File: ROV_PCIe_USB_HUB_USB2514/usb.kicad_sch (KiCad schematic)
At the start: 62 parts, among them J2 61400826021, J3 691311500102, J4 692121430000, J5 61400826021, J6 61400826021, J7 629722000214, U10 TPS2051CDBV, U11 MIC5504-3.3YM5, U12 TPS2116DRL, U13 USB2514B_Bi, U5 TPS2051CDBV, U6 TPS2051CDBV, U8 TS3USB30EDGSR, U9 TPS2051CDBV, Y3 ABM8-24.000MHZ-B2-T

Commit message: updates
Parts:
- C35: Part Number CL21A106KOQNNNE -> CL21A106KOQNNNE
- C36: renamed from C60; Part Number CL05B104KB5NNNC -> CL05B104KO5NNNC
- C37: renamed from C59; Part Number CL05B104KB5NNNC -> CL05B104KO5NNNC
- C38: renamed from C58; Part Number CL05B104KB5NNNC -> CL05B104KO5NNNC
- C39: renamed from C57; Part Number CL05B104KB5NNNC -> CL05B104KO5NNNC
- C40: renamed from C53; Part Number CL21A106KOQNNNE -> CL21A106KOQNNNE
- C41: renamed from C54; Part Number CL05B104KB5NNNC -> CL05B104KO5NNNC
- C42: renamed from C55; Part Number CL05B104KB5NNNC -> CL05B104KO5NNNC
- C43: renamed from C36; Part Number CL21A106KOQNNNE -> CL21A106KOQNNNE
- C44: renamed from C37; Part Number CL21A106KOQNNNE -> CL21A106KOQNNNE
- C45: renamed from C40; Part Number CL05B104KB5NNNC -> CL05B104KO5NNNC
- C46: renamed from C41; Part Number CL21A106KOQNNNE -> CL21A106KOQNNNE
- C48: renamed from C49; value 18p -> 27p
- C49: renamed from C48; value 18p -> 27p
- C50: Part Number CL05B104KB5NNNC -> CL05B104KO5NNNC
- C51: renamed from C42; Part Number CL21A106KOQNNNE -> CL21A106KOQNNNE
- C52: renamed from C51; Part Number CL05B104KB5NNNC -> CL05B104KO5NNNC
- C53: renamed from C43; Part Number CL21A106KOQNNNE -> CL21A106KOQNNNE
- C54: renamed from C44; footprint Capacitor_SMD:C_0805_2012Metric -> Capacitor_SMD:C_0603_1608Metric; Part Number CL21B105KOFNNNE -> CL10B105KO8NNNC
- C55: renamed from C45; Part Number CL21A106KOQNNNE -> CL21A106KOQNNNE
- C56: renamed from C46; footprint Capacitor_SMD:C_0805_2012Metric -> Capacitor_SMD:C_0603_1608Metric; Part Number CL21B105KOFNNNE -> CL10B105KO8NNNC
- C57: renamed from C47; footprint Capacitor_SMD:C_0805_2012Metric -> Capacitor_SMD:C_0603_1608Metric; Part Number CL21B105KOFNNNE -> CL10B105KO8NNNC
- J3: renamed from J2; value 61400826021 -> USB-A-D-RA; Part Number 61400826021 -> USB-A-D-RA
- J4: value 692121430000 -> USB-A3-S-VT-CS5A; Part Number 692121430000 -> USB-A3-S-VT-CS5A
- J5, J6: value 61400826021 -> USB-A-D-RA; Part Number 61400826021 -> USB-A-D-RA
- R19: renamed from R38; Part Number AC0603FR-0710KL -> RC0603FR-0710KL
- R20: renamed from R19; Part Number AC0603FR-0710KL -> RC0603FR-0710KL
- R21: renamed from R37; value 12.0k 1% -> 12k; Part Number AC0603FR-0710KL -> RC0603FR-0712KL
- R22: renamed from R30; Part Number AC0603FR-0710KL -> RC0603FR-0710KL
- R23: renamed from R24; Part Number AC0603FR-075K1L -> RC0603FR-075K1L
- R24: renamed from R26; Part Number AC0603FR-0710KL -> RC0603FR-0710KL
- R25: Part Number AC0603FR-075K1L -> RC0603FR-075K1L
- R26: renamed from R27; Part Number AC0603FR-07330KL -> RC0603FR-07330KL
- R27: renamed from R28; Part Number AC0603FR-07100KL -> RC0603FR-07100KL
- R28: renamed from R31; Part Number AC0603FR-07470RL -> RC0603FR-07270RL
- R29: renamed from R32; Part Number AC0603FR-07470RL -> RC0603FR-07270RL
- R30: renamed from R29; Part Number AC0603FR-07100KL -> RC0603FR-07100KL
- R31: renamed from R33; Part Number AC0603FR-07470RL -> RC0603FR-07270RL
- R32: renamed from R36; Part Number AC0603FR-07470RL -> RC0603FR-07100RL
- R33: renamed from R34; Part Number AC0603FR-07470RL -> RC0603FR-07270RL
- R34: renamed from R35; Part Number AC0603FR-07470RL -> RC0603FR-07100RL
- U10, U5, U6, U9: value TPS2051CDBV -> TPS2051CDBVR; Part Number TPS2051CDBV -> TPS2051CDBVR
- U11: value MIC5504-3.3YM5 -> MIC5504-3.3YM5-TR; Part Number MIC5504-3.3YM5 -> MIC5504-3.3YM5-TR
- U8: renamed from U13; value USB2514B_Bi -> USB2514B/M2
- renumbered C52 to C47, D7 to D1, D8 to D2, D9 to D3, D12 to D4, D10 to D5, D11 to D6, FB3 to FB2, J3 to J2, U8 to U7, Y3 to Y2

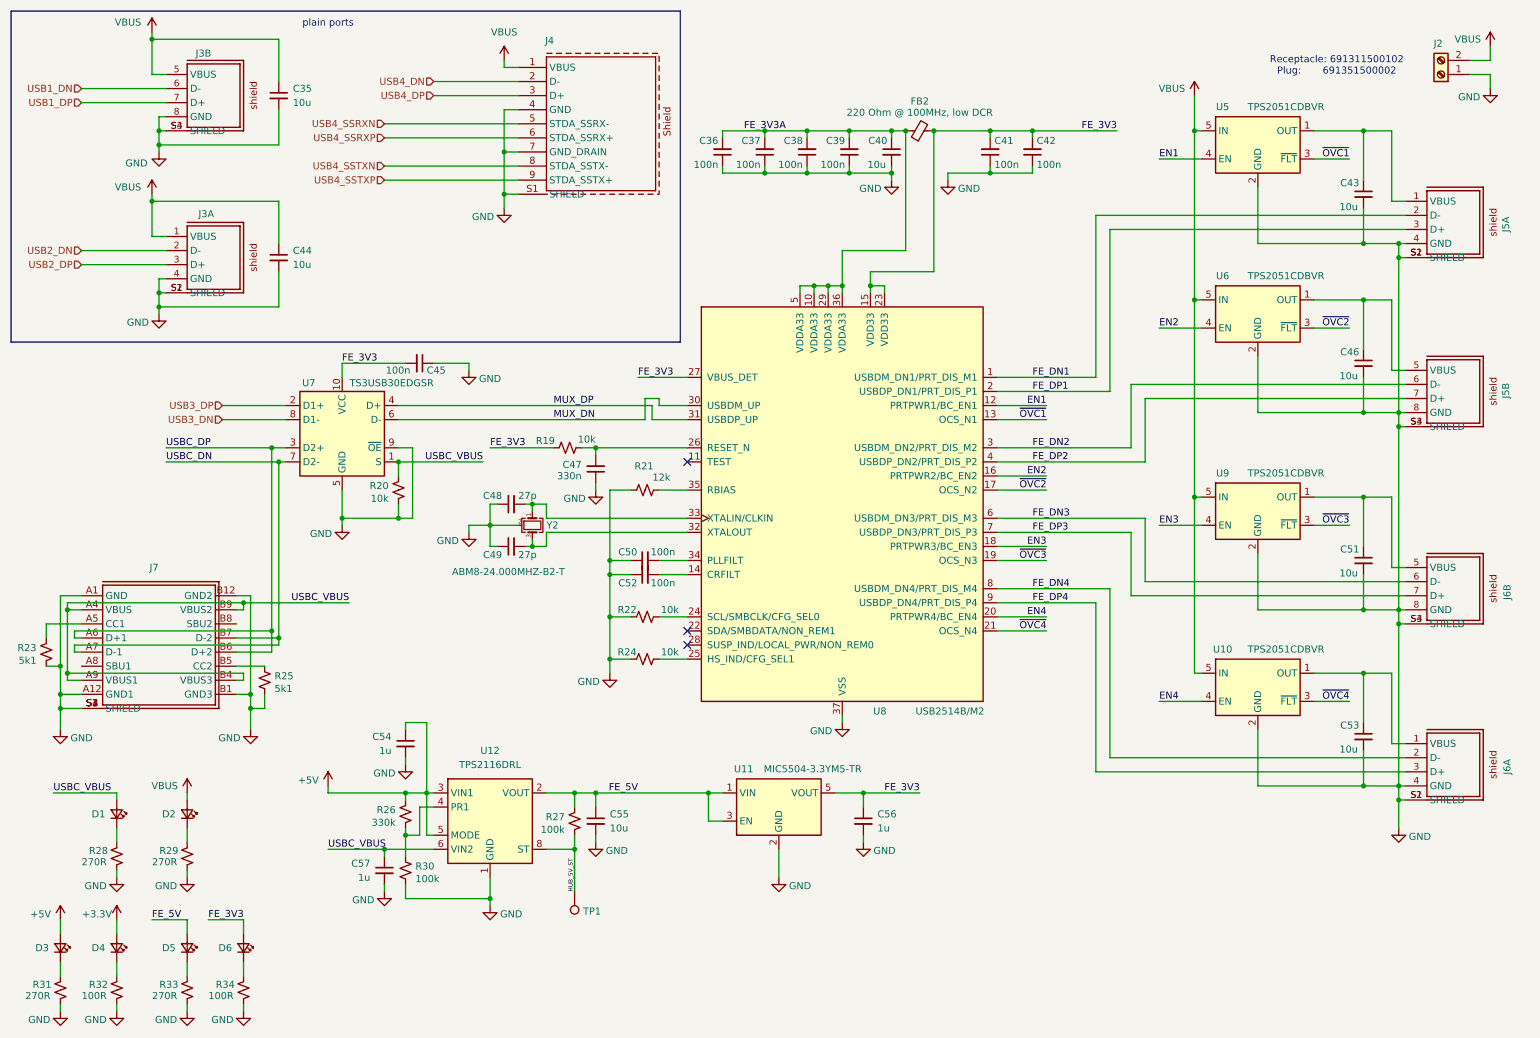
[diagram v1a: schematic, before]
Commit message: updates (fe1.1s board deprecated)
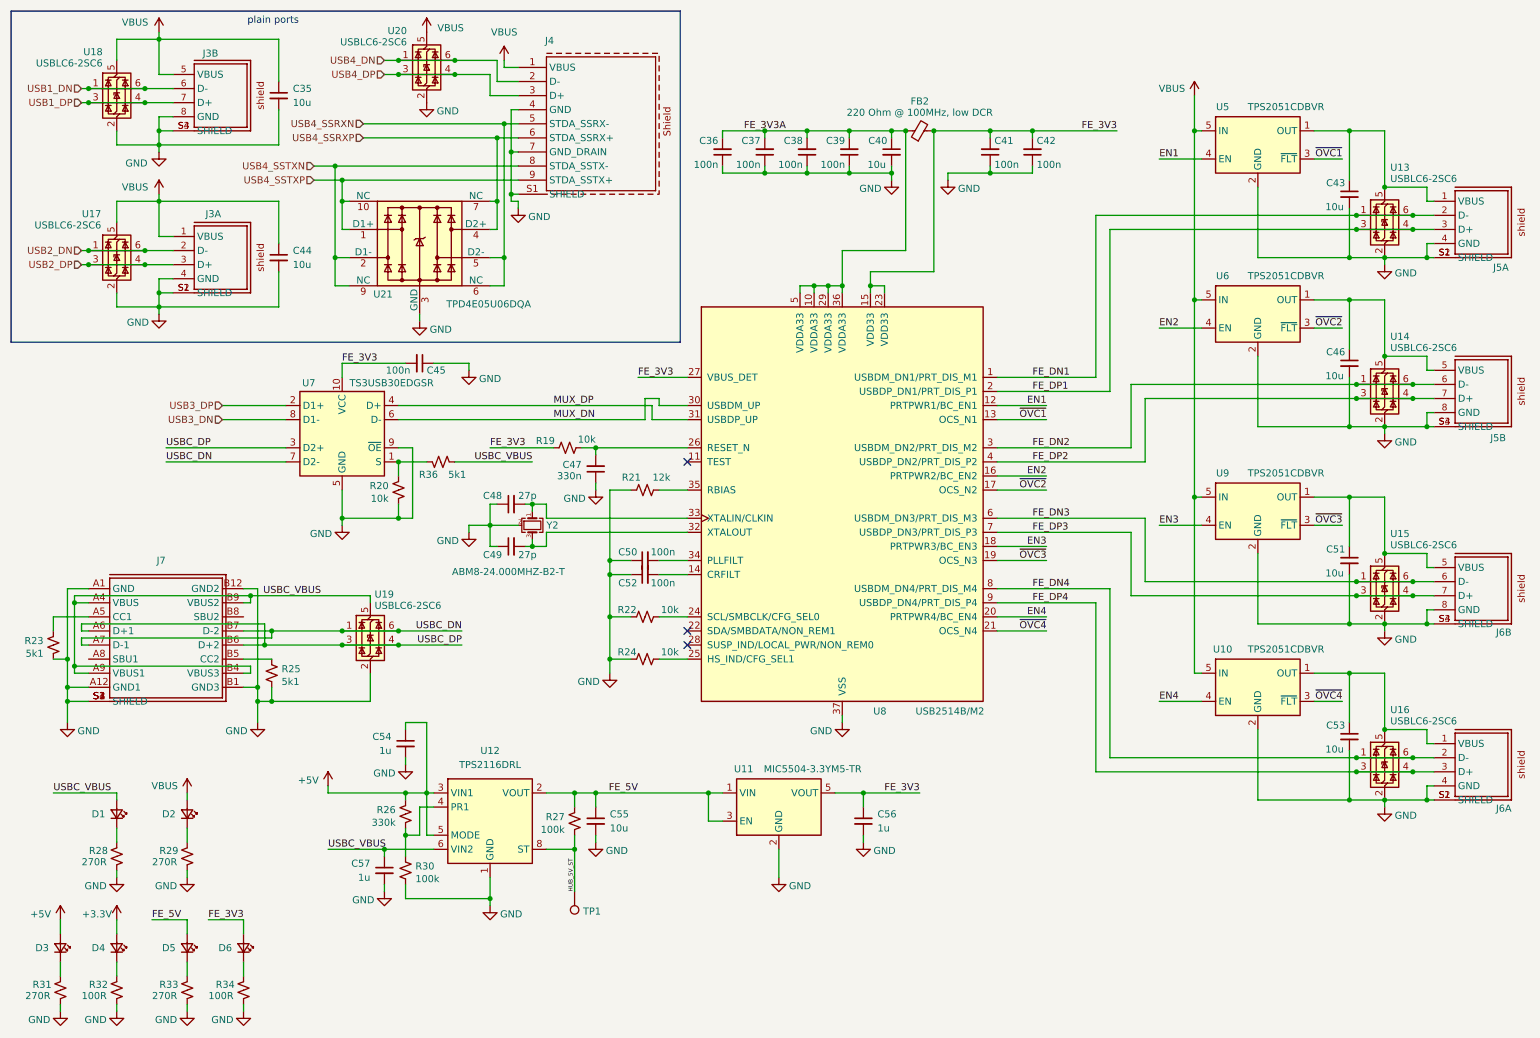
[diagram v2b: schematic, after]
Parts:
- removed J2: 691311500102, Connector_THT_Wurth:J_Wurth_WR-TBL_691311500102, symbol Connector:Screw_Terminal_01x02
- added R36: 5k1, Resistor_SMD:R_0603_1608Metric, symbol Device:R_Small_US
- added U13, U14, U15, U16, U17, U18, U19, U20: USBLC6-2SC6, Package_TO_SOT_SMD:SOT-23-6, symbol Power_Protection:USBLC6-2SC6
- added U21: TPD4E05U06DQA, Package_SON:USON-10_2.5x1.0mm_P0.5mm, symbol Power_Protection:TPD4E05U06DQA
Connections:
- net FE_DN1: now also U13.1 (I/O1), U13.6 (I/O1)
- net FE_DN2: now also U14.1 (I/O1), U14.6 (I/O1)
- net FE_DN3: now also U15.1 (I/O1), U15.6 (I/O1)
- net FE_DN4: now also U16.1 (I/O1), U16.6 (I/O1)
- net FE_DP1: now also U13.3 (I/O2), U13.4 (I/O2)
- net FE_DP2: now also U14.3 (I/O2), U14.4 (I/O2)
- net FE_DP3: now also U15.3 (I/O2), U15.4 (I/O2)
- net FE_DP4: now also U16.3 (I/O2), U16.4 (I/O2)
- net GND: now also U13.2 (GND), U14.2 (GND), U15.2 (GND), U16.2 (GND), U17.2 (GND), U18.2 (GND), U19.2 (GND), U20.2 (GND), U21.3 (GND), U21.8 (GND)
- net USB1_DN: now also U18.1 (I/O1), U18.6 (I/O1)
- net USB1_DP: now also U18.3 (I/O2), U18.4 (I/O2)
- net USB2_DN: now also U17.1 (I/O1), U17.6 (I/O1)
- net USB2_DP: now also U17.3 (I/O2), U17.4 (I/O2)
- net USB4_DN: now also U20.1 (I/O1), U20.6 (I/O1)
- net USB4_DP: now also U20.3 (I/O2), U20.4 (I/O2)
- net USB4_SSRXN: now also U21.5 (D2-), U21.6 (NC)
- net USB4_SSRXP: now also U21.4 (D2+), U21.7 (NC)
- net USB4_SSTXN: now also U21.2 (D1-), U21.9 (NC)
- net USB4_SSTXP: now also U21.1 (D1+), U21.10 (NC)
- net USBC_DN: now also U19.1 (I/O1), U19.6 (I/O1)
- net USBC_DP: now also U19.3 (I/O2), U19.4 (I/O2)
- net USBC_VBUS: now also R36.1, U19.5 (VBUS); no longer R20.2, U7.1 (S)
- net VBUS: now also U17.5 (VBUS), U18.5 (VBUS), U20.5 (VBUS)
- net at C53.1, J6.1 (VBUS), U10.1 (OUT): now also U16.5 (VBUS)
- net at C51.1, J6.5 (VBUS), U9.1 (OUT): now also U15.5 (VBUS)
- net at C46.1, J5.5 (VBUS), U6.1 (OUT): now also U14.5 (VBUS)
- net at C43.1, J5.1 (VBUS), U5.1 (OUT): now also U13.5 (VBUS)
- new net: R20.2, R36.2, U7.1 (S)
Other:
- note removed: "Receptacle: 691311500102 Plug: 691351500002"
- moved on the sheet: C43, C46, C51, C53, J3A, J3B, J5A, J5B, J6A, J6B, J7, R23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

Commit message: changes
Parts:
- C35, C40, C43, C44, C46, C51, C53, C55: Part Number CL21A106KOQNNNE -> CC0805KRX5R8BB106
- C36, C37, C38, C39, C41, C42, C45, C50, C52: Part Number CL05B104KO5NNNC -> CC0402KRX7R8BB104
- C47: Part Number CL05A334KQ5NNNC -> CC0402KPX5R6BB334
- C48, C49: Part Number CL05C180JB5NNNC -> CC0402JRNPO9BN270
- C54, C56, C57: Part Number CL10B105KO8NNNC -> CC0603KRX7R8BB105
- R21: value 12k -> 12k 1%
- R26: value 330k -> 10k; Part Number RC0603FR-07330KL -> RC0603FR-0710KL
- R30: value 100k -> 5k1; Part Number RC0603FR-07100KL -> RC0603FR-075K1L
- R36: Part Number RC0603FR-0710KL -> RC0603FR-075K1L
- U13, U14, U15, U16, U17, U18, U19, U20: Part Number (none) -> USBLC6-2SC6
- U21: Part Number (none) -> TPD4E05U06DQA
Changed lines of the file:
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@@
 			)
 		)
-		(property "Value" "330k"
+		(property "Value" "10k"
 			(at 82.042 159.004 0)
 			(show_name no)
@@
 			)
 		)
-		(property "Part Number" "RC0603FR-07330KL"
+		(property "Part Number" "RC0603FR-0710KL"
 			(at 83.82 157.48 0)
 			(hide yes)
@@
 			)
 		)
+		(property "Part Number" "USBLC6-2SC6"
+			(at 260.35 147.32 0)
+			(hide yes)
+			(show_name no)
+			(do_not_autoplace no)
+			(effects
+				(font
+					(size 1.27 1.27)
+				)
+			)
+		)
 		(pin "1"
 		)
@@
 			)
 		)
-		(property "Part Number" "CL05B104KO5NNNC"
+		(property "Part Number" "CC0402KRX7R8BB104"
 			(at 148.59 38.1 0)
 			(hide yes)
@@
 			)
 		)
-		(property "Part Number" "CL10B105KO8NNNC"
+		(property "Part Number" "CC0603KRX7R8BB105"
 			(at 166.37 158.75 0)
 			(hide yes)
@@
 			)
 		)
-		(property "Part Number" "CL21A106KOQNNNE "
+		(property "Part Number" "CC0805KRX5R8BB106"
 			(at 60.96 27.94 0)
 			(hide yes)
@@
 			)
 		)
-		(property "Part Number" "CL21A106KOQNNNE "
+		(property "Part Number" "CC0805KRX5R8BB106"
 			(at 254 143.51 0)
 			(hide yes)
@@
 			)
 		)
-		(property "Part Number" "CL05B104KO5NNNC"
+		(property "Part Number" "CC0402KRX7R8BB104"
 			(at 196.85 38.1 0)
 			(hide yes)
@@
 			)
 		)
+		(property "Part Number" "USBLC6-2SC6"
+			(at 260.35 80.01 0)
+			(hide yes)
+			(show_name no)
+			(do_not_autoplace no)
+			(effects
+				(font
+					(size 1.27 1.27)
+				)
+			)
+		)
 		(pin "1"
 		)
@@
 			)
 		)
-		(property "Part Number" "CL05A334KQ5NNNC"
+		(property "Part Number" "CC0402KPX5R6BB334"
 			(at 118.11 95.25 0)
 			(hide yes)
@@
 			)
 		)
-		(property "Part Number" "CL05B104KO5NNNC"
+		(property "Part Number" "CC0402KRX7R8BB104"
 			(at 156.21 38.1 0)
 			(hide yes)
@@
 			)
 		)
-		(property "Part Number" "CL05C180JB5NNNC"
+		(property "Part Number" "CC0402JRNPO9BN270"
 			(at 102.87 109.22 0)
 			(hide yes)
@@
 			)
 		)
-		(property "Part Number" "CL21A106KOQNNNE "
+		(property "Part Number" "CC0805KRX5R8BB106"
 			(at 254 76.2 0)
 			(hide yes)
@@
 			)
 		)
-		(property "Part Number" "CL21A106KOQNNNE "
+		(property "Part Number" "CC0805KRX5R8BB106"
 			(at 118.11 158.75 0)
 			(hide yes)
@@
 			)
 		)
+		(property "Part Number" "TPD4E05U06DQA"
+			(at 86.36 54.61 0)
+			(hide yes)
+			(show_name no)
+			(do_not_autoplace no)
+			(effects
+				(font
+					(size 1.27 1.27)
+				)
+			)
+		)
 		(pin "2"
 		)
@@
 			)
 		)
+		(property "Part Number" "USBLC6-2SC6"
+			(at 31.75 55.88 0)
+			(hide yes)
+			(show_name no)
+			(do_not_autoplace no)
+			(effects
+				(font
+					(size 1.27 1.27)
+				)
+			)
+		)
 		(pin "1"
 		)
@@
 			)
 		)
-		(property "Part Number" "CL05B104KO5NNNC"
+		(property "Part Number" "CC0402KRX7R8BB104"
 			(at 127 111.76 0)
 			(hide yes)
@@
 			)
 		)
-		(property "Part Number" "CL05C180JB5NNNC"
+		(property "Part Number" "CC0402JRNPO9BN270"
 			(at 102.87 101.6 0)
 			(hide yes)
@@
 			)
 		)
+		(property "Part Number" "USBLC6-2SC6"
+			(at 260.35 49.53 0)
+			(hide yes)
+			(show_name no)
+			(do_not_autoplace no)
+			(effects
+				(font
+					(size 1.27 1.27)
+				)
+			)
+		)
 		(pin "1"
 		)
@@
 			)
 		)
+		(property "Part Number" "USBLC6-2SC6"
+			(at 260.35 115.57 0)
+			(hide yes)
+			(show_name no)
+			(do_not_autoplace no)
+			(effects
+				(font
+					(size 1.27 1.27)
+				)
+			)
+		)
 		(pin "1"
 		)
@@
 			)
 		)
-		(property "Part Number" "CL21A106KOQNNNE "
+		(property "Part Number" "CC0805KRX5R8BB106"
 			(at 171.45 38.1 0)
 			(hide yes)
@@
 			)
 		)
-		(property "Part Number" "CL21A106KOQNNNE "
+		(property "Part Number" "CC0805KRX5R8BB106"
 			(at 60.96 57.15 0)
 			(hide yes)
@@
 			)
 		)
-		(property "Part Number" "CL05B104KO5NNNC"
+		(property "Part Number" "CC0402KRX7R8BB104"
 			(at 189.23 38.1 0)
 			(hide yes)
@@
 			)
 		)
+		(property "Part Number" "USBLC6-2SC6"
+			(at 87.63 21.59 0)
+			(hide yes)
+			(show_name no)
+			(do_not_autoplace no)
+			(effects
+				(font
+					(size 1.27 1.27)
+				)
+			)
+		)
 		(pin "1"
 		)
@@
 			)
 		)
+		(property "Part Number" "USBLC6-2SC6"
+			(at 31.75 26.67 0)
+			(hide yes)
+			(show_name no)
+			(do_not_autoplace no)
+			(effects
+				(font
+					(size 1.27 1.27)
+				)
+			)
+		)
 		(pin "1"
 		)
@@
 			)
 		)
-		(property "Part Number" "CL21A106KOQNNNE "
+		(property "Part Number" "CC0805KRX5R8BB106"
 			(at 254 45.72 0)
 			(hide yes)
@@
 			)
 		)
-		(property "Part Number" "CL05B104KO5NNNC"
+		(property "Part Number" "CC0402KRX7R8BB104"
 			(at 127 114.3 0)
 			(hide yes)
@@
 			)
 		)
-		(property "Value" "12k"
+		(property "Value" "12k 1%"
 			(at 131.572 96.774 90)
 			(show_name no)
@@
 			)
 		)
-		(property "Part Number" "RC0603FR-0710KL"
+		(property "Part Number" "RC0603FR-075K1L"
 			(at 90.17 93.98 0)
 			(hide yes)
@@
 			)
 		)
-		(property "Part Number" "CL05B104KO5NNNC"
+		(property "Part Number" "CC0402KRX7R8BB104"
 			(at 140.97 38.1 0)
 			(hide yes)
@@
 			)
 		)
-		(property "Part Number" "CL21A106KOQNNNE "
+		(property "Part Number" "CC0805KRX5R8BB106"
 			(at 254 111.76 0)
 			(hide yes)
@@
 			)
 		)
-		(property "Value" "100k"
+		(property "Value" "5k1"
 			(at 85.598 169.164 0)
 			(show_name no)
@@
 			)
 		)
-		(property "Part Number" "RC0603FR-07100KL"
+		(property "Part Number" "RC0603FR-075K1L"
 			(at 83.82 167.64 0)
 			(hide yes)
@@
 			)
 		)
+		(property "Part Number" "USBLC6-2SC6"
+			(at 77.47 124.46 0)
+			(hide yes)
+			(show_name no)
+			(do_not_autoplace no)
+			(effects
+				(font
+					(size 1.27 1.27)
+				)
+			)
+		)
 		(pin "1"
 		)
@@
 			)
 		)
-		(property "Part Number" "CL05B104KO5NNNC"
+		(property "Part Number" "CC0402KRX7R8BB104"
 			(at 86.36 76.2 0)
 			(hide yes)
@@
 			)
 		)
-		(property "Part Number" "CL10B105KO8NNNC"
+		(property "Part Number" "CC0603KRX7R8BB105"
 			(at 83.82 144.78 0)
 			(hide yes)
@@
 			)
 		)
-		(property "Part Number" "CL10B105KO8NNNC"
+		(property "Part Number" "CC0603KRX7R8BB105"
 			(at 80.01 167.64 0)
 			(hide yes)
@@
 			)
 		)
-		(property "Part Number" "CL05B104KO5NNNC"
+		(property "Part Number" "CC0402KRX7R8BB104"
 			(at 163.83 38.1 0)
 			(hide yes)

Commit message: final
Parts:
- J8: renamed from J7; value 629722000214 -> USB4085-GF-A; Part Number 629722000214 -> USB4085-GF-A
- U21: renamed from U12; value TPS2116DRL -> TPS2116DRLR; Part Number TPS2116DRL -> TPS2116DRLR
- U9: renamed from U21; value TPD4E05U06DQA -> TPD4E05U06DQAR; Part Number TPD4E05U06DQA -> TPD4E05U06DQAR
- renumbered D1 to D3, D2 to D4, D3 to D5, D4 to D6, D5 to D7, D6 to D8, J3 to J4, J4 to J5, J5 to J6, J6 to J7, R19 to R20, R36 to R21, R20 to R22, R21 to R23, R22 to R24, R23 to R25, R24 to R26, R25 to R27, R26 to R28, R27 to R29, R28 to R30, R29 to R31, R30 to R32, R31 to R33, R32 to R34, R33 to R35, R34 to R36, U17 to U10, U6 to U11, U14 to U12, U7 to U13, U8 to U14, U9 to U15, U15 to U16, U19 to U17, U10 to U18, U16 to U19, U11 to U20, U20 to U5, U18 to U6, U5 to U7, U13 to U8

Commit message: changes
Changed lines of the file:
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@@
 	)
 	(symbol
+		(lib_name "61400826021_2")
 		(lib_id "Connector_Wurth_WR-USB:61400826021")
 		(at 49.53 57.15 0)
@@
 	)
 	(symbol
+		(lib_name "61400826021_1")
 		(lib_id "Connector_Wurth_WR-USB:61400826021")
 		(at 49.53 27.94 0)
@@
 		(dnp no)
 		(property "Reference" "J4"
-			(at 47.244 20.32 0)
+			(at 47.752 20.066 0)
 			(show_name no)
 			(do_not_autoplace no)

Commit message: changes
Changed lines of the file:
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@@
 		)
 		(property "Value" "MIC5504-3.3YM5-TR"
-			(at 157.226 149.352 0)
+			(at 158.75 149.352 0)
 			(show_name no)
 			(do_not_autoplace no)
